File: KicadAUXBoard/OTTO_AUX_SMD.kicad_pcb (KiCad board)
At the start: 2 copper layers, 297 x 92 mm, 203 parts, among them CN203 Conn_01x06, J1_KD028QVFMA17 Conn_02x25_Counter_Clockwise, SW1 ALPS SKHC, SW10 ALPS SKHC, SW11 ALPS SKHC, SW12 ALPS SKHC, SW13 ALPS SKHC, SW14 ALPS SKHC, SW15 ALPS SKHC, SW16 ALPS SKHC, SW17 ALPS SKHC, SW18 ALPS SKHC, SW19 ALPS SKHC, SW2 ALPS SKHC, SW20 ALPS SKHC, SW21 ALPS SKHC, SW22 ALPS SKHC, SW23 ALPS SKHC, SW24 ALPS SKHC, SW25 ALPS SKHC, SW26 ALPS SKHC, SW27 6x6x13mm, SW28 6x6x13mm, SW29 6x6x13mm, SW3 ALPS SKHC, SW30 6x6x13mm, SW31 6x6x13mm, SW32 6x6x13mm, SW33 6x6x13mm, SW34 6x6x13mm, SW35 6x6x13mm, SW36 6x6x13mm, SW37 6x6x13mm, SW38 6x6x13mm, SW39 6x6x13mm, SW4 ALPS SKHC, SW40 6x6x13mm, SW41 6x6x13mm, SW42 6x6x13mm, SW43 6x6x13mm, SW44 6x6x13mm, SW45 6x6x13mm, SW46 6x6x13mm, SW47 6x6x13mm, SW5 ALPS SKHC, SW50 6x6x13mm, SW51 6x6x13mm, SW52 6x6x13mm, SW53 6x6x13mm, SW54 6x6x13mm, SW55 6x6x13mm, SW56 6x6x13mm, SW6 ALPS SKHC, SW7 ALPS SKHC, SW8 ALPS SKHC, SW9 ALPS SKHC, U1 SN74LV1T34_SOT-23_A

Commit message: [AUX] Expand SKHC footprints and move lower keys down
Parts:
- moved LED1 2.04 mm to (54.0, 181.8)
- moved LED10 2.04 mm to (216.0, 181.8)
- moved LED11 2.04 mm to (234.0, 181.8)
- moved LED12 2.04 mm to (252.0, 181.8)
- moved LED13 2.04 mm to (270.0, 181.8)
- moved LED14 2.04 mm to (288.0, 181.8)
- moved LED15 2.04 mm to (306.0, 181.8)
- moved LED16 2.04 mm to (324.0, 181.8)
- moved LED2 2.04 mm to (72.0, 181.8)
- moved LED3 2.04 mm to (90.0, 181.8)
- moved LED4 2.04 mm to (108.0, 181.8)
- moved LED5 2.04 mm to (126.0, 181.8)
- moved LED6 2.04 mm to (144.0, 181.8)
- moved LED7 2.04 mm to (162.0, 181.8)
- moved LED8 2.04 mm to (180.0, 181.8)
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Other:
- outline, holes or cut-outs redrawn

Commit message: Screen backlight control (+more)
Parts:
- moved H201 3.00 mm to (44.8, 195.2)
- moved H202 3.00 mm to (333.2, 195.2)
- moved DISPLAY1 2.96 mm to (207.1, 120.3)
- moved J1_KD028QVFMA17 2.96 mm to (216.9, 132.7)
- moved C78 2.92 mm to (56.6, 169.3)
- moved R11 2.92 mm to (63.5, 168.8)
- moved R208 2.92 mm to (63.5, 166.9)
- moved R27 2.92 mm to (63.5, 170.7)
- moved U1 2.92 mm to (59.6, 169.3)
- moved C1 2.00 mm to (54.0, 177.0)
- moved C10 2.00 mm to (216.0, 177.0)
- moved C11 2.00 mm to (234.0, 177.0)
- moved C12 2.00 mm to (252.0, 177.0)
- moved C13 2.00 mm to (270.0, 177.0)
- moved C14 2.00 mm to (288.0, 177.0)
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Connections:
- LED17 pad 4: /MCU/LEDS/LED_IN -> (no net)
- LED26 pad 1: /MCU/LEDS/LED_CONN1 -> (no net)
- LED27 pad 4: /MCU/LEDS/LED_CONN2 -> (no net)
- LED35 pad 1: Net-(LED34-Pad4) -> (no net)
- LED38 pad 4: Net-(LED38-Pad4) -> (no net)
- LED40 pad 1: Net-(LED39-Pad4) -> (no net)
- LED47 pad 1: /MCU/LEDS/LED_CONN3 -> (no net)
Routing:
- net (no net): track 0.00 -> 492.8 mm
- net /MCU/LEDS/LED_CONN1: track 259.7 -> 0.00 mm
- net /MCU/LEDS/LED_CONN2: track 89.2 -> 0.00 mm
- net /MCU/LEDS/LED_CONN3: track 85.9 -> 0.00 mm
- net Net-(LED38-Pad4): track 22.9 -> 0.00 mm
- net Net-(LED39-Pad4): track 16.9 -> 0.00 mm
- net Net-(LED34-Pad4): track 16.9 -> 0.00 mm
- net GND: track 0.00 -> 3.78 mm
- net +5V_LEDS: track 263.4 -> 265.1 mm
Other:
- board size 297 x 92 mm -> 297 x 95 mm

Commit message: 3d models
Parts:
- removed CN203: Conn_01x06, Connector_PinSocket_2.54mm:PinSocket_1x06_P2.54mm_Vertical
- removed JP1, JP2, JP3: Jumper_2_Open, Jumper:SolderJumper-2_P1.3mm_Open_TrianglePad1.0x1.5mm
- removed R27: 100, Resistor_SMD:R_0805_2012Metric_Pad1.15x1.40mm_HandSolder
- removed TP1: TestPoint, TestPoint:TestPoint_THTPad_D2.0mm_Drill1.0mm
- added C49: 47uF, Capacitor_SMD:C_1206_3216Metric, F.Cu at (56.2, 51.4)
- added C50: 10nF, Capacitor_SMD:C_0805_2012Metric_Pad1.15x1.40mm_HandSolder, F.Cu at (61.4, 51.2)
- added J1: Conn_02x05_Odd_Even, Connector_PinHeader_1.27mm:PinHeader_2x05_P1.27mm_Vertical, B.Cu at (22.7, 77.8)
- added J2: Conn_02x05_Odd_Even, Connector_PinHeader_1.27mm:PinHeader_2x05_P1.27mm_Vertical, B.Cu at (217.9, 74.6)
- added Q1: AO3400A, Package_TO_SOT_SMD:SOT-23, F.Cu at (208.8, 69.5)
- added R1: 47k, Resistor_SMD:R_0805_2012Metric_Pad1.15x1.40mm_HandSolder, F.Cu at (211.6, 69.5)
- added R2: 90, Resistor_SMD:R_0805_2012Metric_Pad1.15x1.40mm_HandSolder, F.Cu at (213.7, 65.1)
- added R3: 100k, Resistor_SMD:R_0805_2012Metric_Pad1.15x1.40mm_HandSolder, F.Cu at (66.1, 51.2)
- added R4: 0, Resistor_SMD:R_0805_2012Metric_Pad1.15x1.40mm_HandSolder, F.Cu at (60.5, 59.1)
- added R5: 90, Resistor_SMD:R_0805_2012Metric_Pad1.15x1.40mm_HandSolder, F.Cu at (203.7, 65.1)
- added R6: 90, Resistor_SMD:R_0805_2012Metric_Pad1.15x1.40mm_HandSolder, F.Cu at (205.7, 65.1)
- added R7: 90, Resistor_SMD:R_0805_2012Metric_Pad1.15x1.40mm_HandSolder, F.Cu at (207.7, 65.1)
- added R8: 90, Resistor_SMD:R_0805_2012Metric_Pad1.15x1.40mm_HandSolder, F.Cu at (209.7, 65.1)
- added R9: 90, Resistor_SMD:R_0805_2012Metric_Pad1.15x1.40mm_HandSolder, F.Cu at (211.7, 65.1)
- added U2: TPS22918_SOT23-6_A, OTTO_Footprints_Lib:SOT-23-6, F.Cu at (55.8, 55.3)
- moved C1 98.9 mm to (26.2, 82.1)
- moved C10 98.9 mm to (188.2, 82.1)
- moved C100 98.9 mm to (231.2, 16.9)
- moved C101 98.9 mm to (243.2, 16.9)
- moved C102 98.9 mm to (255.2, 16.9)
- moved C103 98.9 mm to (267.2, 16.9)
- moved C104 98.9 mm to (285.2, 16.9)
- moved C105 98.9 mm to (297.2, 16.9)
- moved C11 98.9 mm to (206.2, 82.1)
- moved C12 98.9 mm to (224.2, 82.1)
- moved C13 98.9 mm to (242.2, 82.1)
- moved C14 98.9 mm to (260.2, 82.1)
- moved C15 98.9 mm to (278.2, 82.1)
- moved C16 98.9 mm to (296.2, 82.1)
- moved C17 98.9 mm to (53.2, 67.1)
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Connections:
- net /MCU/LEDS/SPI_MOSI_MCU_5V renamed /LEDs/SPI_MOSI_MCU_5V
- J1_KD028QVFMA17 pad 43: BL_PWM -> 5V_BACKLIGHT
- J1_KD028QVFMA17 pad 44: GND -> Net-(J1_KD028QVFMA17-Pad44)
- J1_KD028QVFMA17 pad 45: GND -> Net-(J1_KD028QVFMA17-Pad45)
- J1_KD028QVFMA17 pad 46: GND -> Net-(J1_KD028QVFMA17-Pad46)
- J1_KD028QVFMA17 pad 47: GND -> Net-(J1_KD028QVFMA17-Pad47)
- J1_KD028QVFMA17 pad 48: GND -> Net-(J1_KD028QVFMA17-Pad48)
- J1_KD028QVFMA17 pad 49: GND -> Net-(J1_KD028QVFMA17-Pad49)
- LED1 pad 4: /MCU/LEDS/LED_CONN1 -> /LEDs/LED_CONN1
- LED16 pad 1: /MCU/LEDS/LED_CONN2 -> /LEDs/LED_CONN2
- LED17 pad 4: (no net) -> /LEDs/LED_IN
- LED26 pad 1: (no net) -> /LEDs/LED_CONN1
- LED27 pad 4: (no net) -> /LEDs/LED_CONN2
- LED35 pad 1: (no net) -> Net-(LED34-Pad4)
- LED38 pad 4: (no net) -> Net-(LED38-Pad4)
- LED40 pad 1: (no net) -> Net-(LED39-Pad4)
- LED47 pad 1: (no net) -> /LEDs/LED_CONN3
- LED48 pad 4: /MCU/LEDS/LED_CONN3 -> /LEDs/LED_CONN3
- LED54 pad 1: /MCU/LEDS/LED_OUT -> (no net)
- R208 pad 1: /MCU/LEDS/LED_IN -> /LEDs/LED_IN
- U1 pad 2: (no net) -> /SPI_MOSI_MCU
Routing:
- net (no net): track 492.8 -> 0.05 mm
- net /LEDs/LED_CONN1: track 0.00 -> 268.3 mm
- net /LEDs/LED_CONN2: track 0.00 -> 90.1 mm
- net /LEDs/LED_CONN3: track 0.00 -> 85.9 mm
- net 5V_BACKLIGHT: track 0.00 -> 58.3 mm
- net 3V3: track 0.00 -> 58.1 mm, vias 0 -> 1
- net GND: track 3.78 -> 61.1 mm, vias 0 -> 14
- net Net-(J1_KD028QVFMA17-Pad49): track 0.00 -> 51.0 mm, vias 0 -> 1
- net Net-(J1_KD028QVFMA17-Pad48): track 0.00 -> 49.3 mm, vias 0 -> 1
- net Net-(J1_KD028QVFMA17-Pad47): track 0.00 -> 47.7 mm, vias 0 -> 1
- net SPI_MOSI_RASPI: track 0.00 -> 46.7 mm
- net Net-(J1_KD028QVFMA17-Pad46): track 0.00 -> 46.1 mm, vias 0 -> 1
- net Net-(J1_KD028QVFMA17-Pad45): track 0.00 -> 44.4 mm, vias 0 -> 1
- net SPI_SCLK_RASPI: track 0.00 -> 44.4 mm
- net SPI_CS_RASPI: track 0.00 -> 43.3 mm
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- added copper zone on B.Cu, net GND
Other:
- outline, holes or cut-outs redrawn
- board text removed: "BOOT 0/1"
- board text removed: "JTAG/SWD"
- board text removed: "PO PI/LED"
- board text removed: "STATUS"

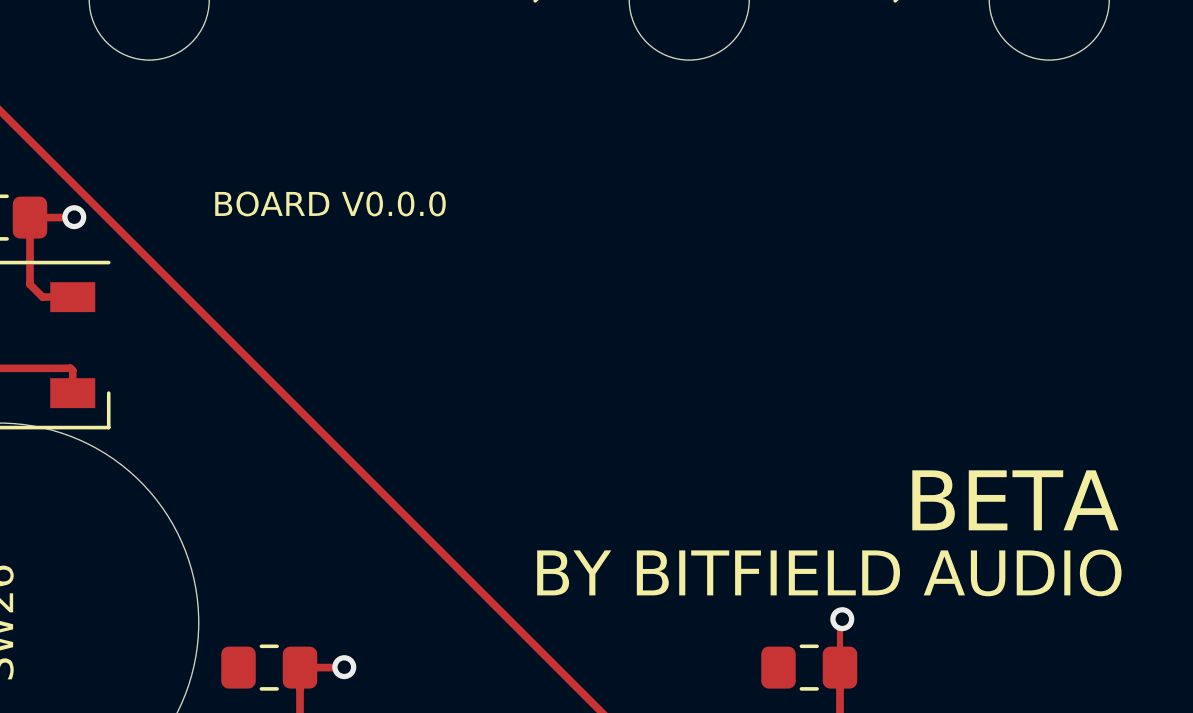
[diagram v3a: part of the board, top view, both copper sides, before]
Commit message: Add simple front pnael
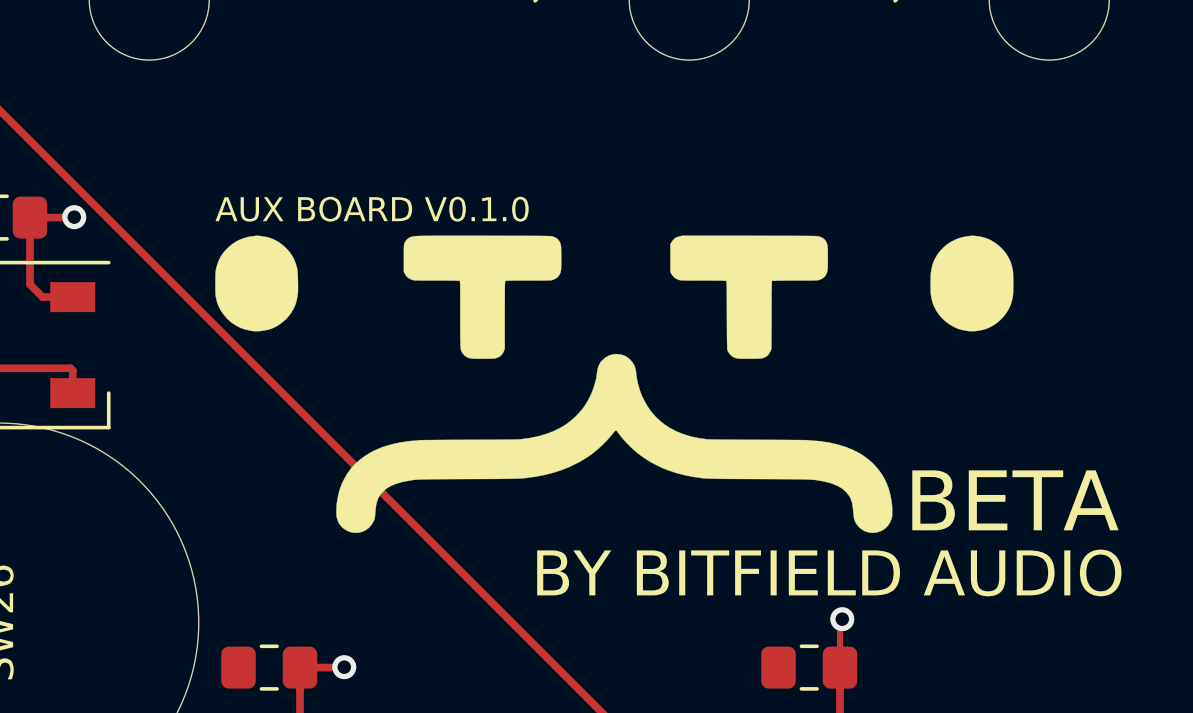
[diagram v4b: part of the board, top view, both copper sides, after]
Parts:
- added G***: otto_logo, OTTO_Footprints_Lib:otto_logo_small, F.Cu at (289.8, 72.8)
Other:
- board text added: "AUX BOARD V0.1.0"
- board text removed: "BOARD V0.0.0"

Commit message: Added front panel and shrunk board width
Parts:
- removed G***: otto_logo, OTTO_Footprints_Lib:otto_logo_small
- moved H213 106.2 mm to (-65.5, 98.1)
- moved J2 105.7 mm to (132.5, 12.4), turned to 270 degrees
- moved R1 96.6 mm to (129.6, 18.4), turned to 0 degrees
- moved Q1 96.3 mm to (125.8, 20.6), turned to 0 degrees
- moved R2 95.1 mm to (129.6, 20.6), turned to 180 degrees
- moved R9 92.4 mm to (129.6, 22.6), turned to 180 degrees
- moved R8 89.7 mm to (129.6, 24.6), turned to 180 degrees
- moved R7 87.1 mm to (129.6, 26.6), turned to 180 degrees
- moved R6 84.4 mm to (129.6, 28.6), turned to 180 degrees
- moved R5 81.7 mm to (129.6, 30.6), turned to 180 degrees
- moved H215 77.4 mm to (-58.5, 98.1)
- moved C48 73.6 mm to (130.1, 48.1), turned to 180 degrees
- moved J1_KD028QVFMA17 43.8 mm to (145.3, 39.9)
- moved R3 39.2 mm to (30.3, 67.0), turned to 90 degrees
- moved C50 33.8 mm to (33.2, 70.0), turned to 180 degrees
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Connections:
- J1 pad 3: LED_PWR_EN -> /SPI_MOSI_MCU
- J1 pad 4: /SPI_MOSI_MCU -> LED_PWR_EN
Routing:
- net Net-(J1_KD028QVFMA17-Pad49): track 51.0 -> 17.1 mm
- net Net-(J1_KD028QVFMA17-Pad48): track 49.3 -> 16.5 mm
- net Net-(J1_KD028QVFMA17-Pad47): track 47.7 -> 15.9 mm
- net 5V_BACKLIGHT: track 58.3 -> 27.3 mm
- net Net-(J1_KD028QVFMA17-Pad46): track 46.1 -> 15.3 mm
- net Net-(J1_KD028QVFMA17-Pad45): track 44.4 -> 14.6 mm
- net Net-(J1_KD028QVFMA17-Pad44): track 42.8 -> 14.0 mm
- net 3V3: track 58.1 -> 77.7 mm
- net /SPI_MOSI_MCU: track 0.00 -> 18.9 mm
- net +5V_REG: track 0.00 -> 16.6 mm
- net LED_PWR_EN: track 0.00 -> 15.8 mm, vias 0 -> 1
- net +5V_LEDS: track 265.1 -> 278.5 mm, vias 54 -> 57
- net BL_PWM: track 6.41 -> 18.0 mm
- net /LEDs/SPI_MOSI_MCU_5V: track 0.00 -> 7.63 mm
- net SPI_MOSI_RASPI: track 46.7 -> 41.8 mm
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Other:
- board size 297 x 95 mm -> 288.5 x 95 mm
- board text removed: "SCREEN"

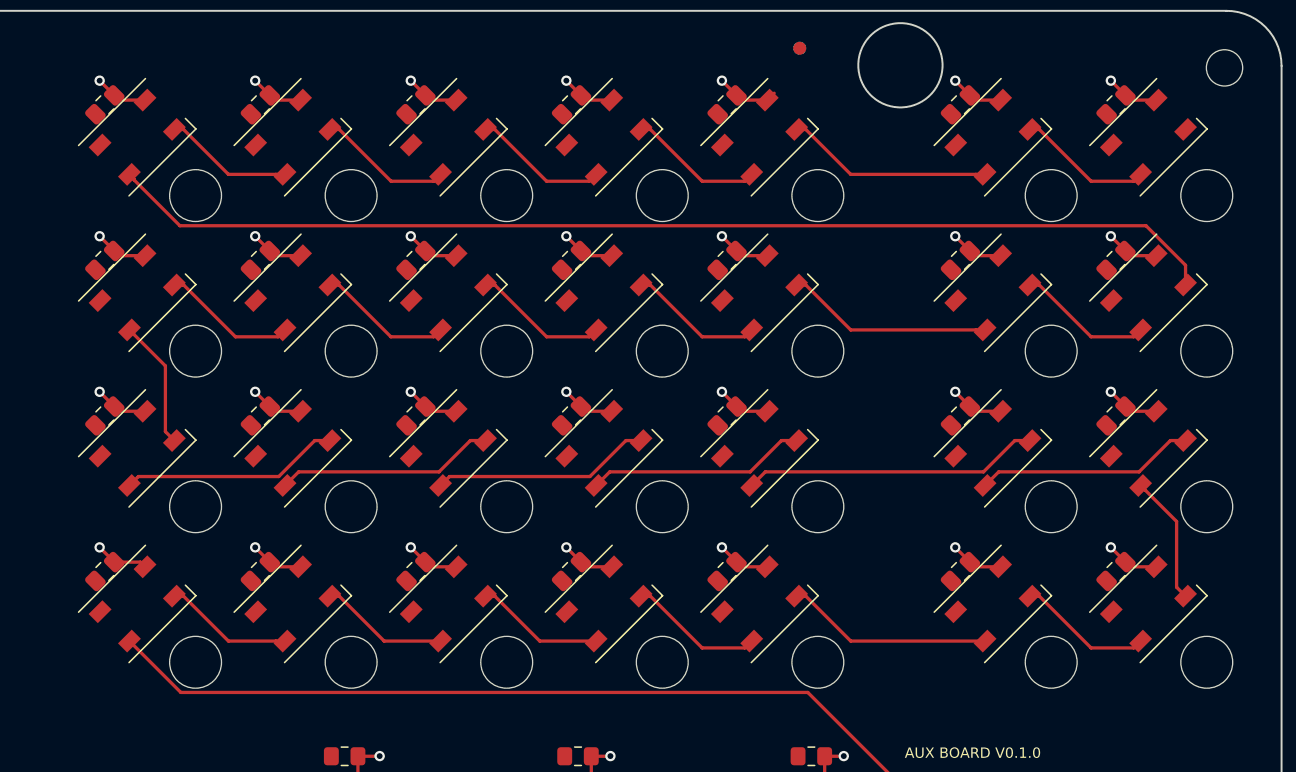
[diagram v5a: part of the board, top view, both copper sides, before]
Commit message: Moved LEDs closer to buttons
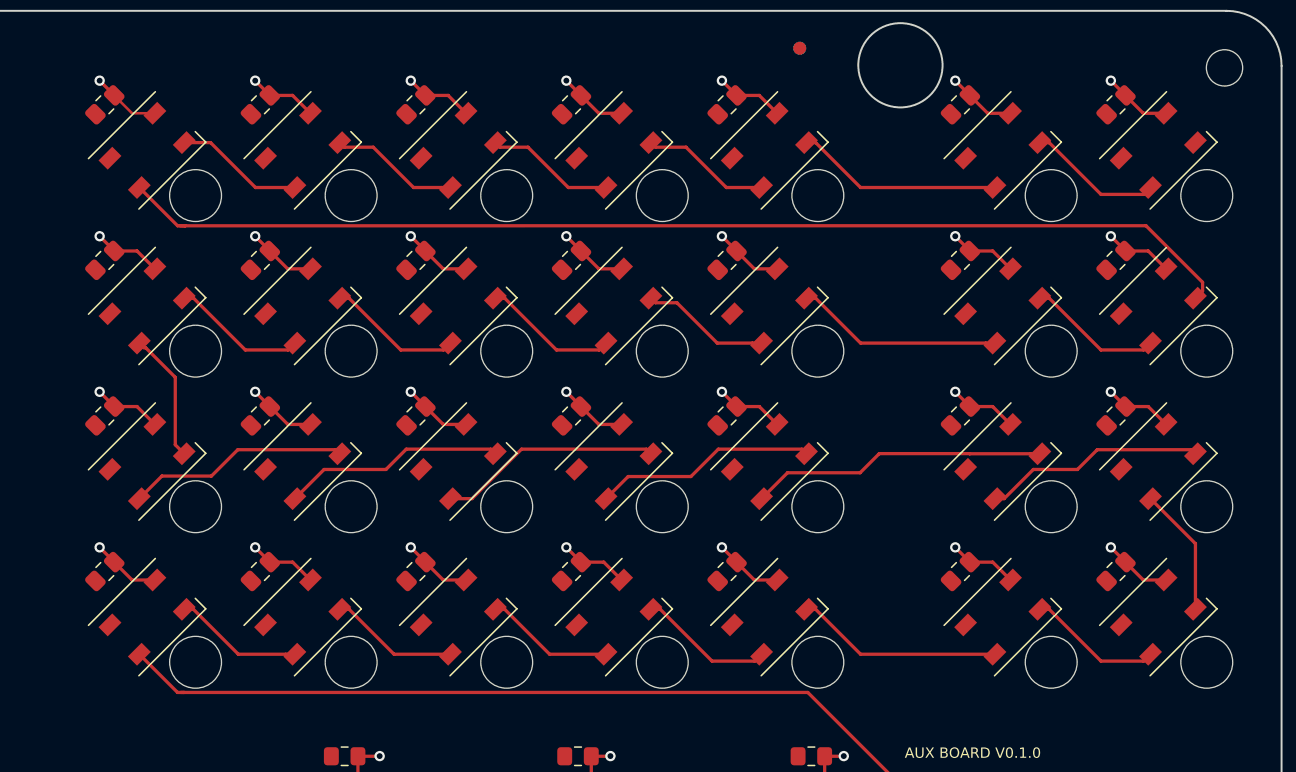
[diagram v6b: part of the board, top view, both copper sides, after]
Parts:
- moved LED27 1.27 mm to (218.0, 56.4)
- moved LED28 1.27 mm to (230.0, 56.4)
- moved LED29 1.27 mm to (242.0, 56.4)
- moved LED30 1.27 mm to (254.0, 56.4)
- moved LED31 1.27 mm to (266.0, 56.4)
- moved LED32 1.27 mm to (284.0, 56.4)
- moved LED33 1.27 mm to (296.0, 56.4)
- moved LED34 1.27 mm to (218.0, 44.4)
- moved LED35 1.27 mm to (230.0, 44.4)
- moved LED36 1.27 mm to (242.0, 44.4)
- moved LED37 1.27 mm to (254.0, 44.4)
- moved LED38 1.27 mm to (266.0, 44.4)
- moved LED39 1.27 mm to (284.0, 44.4)
- moved LED40 1.27 mm to (296.0, 44.4)
- moved LED41 1.27 mm to (218.0, 32.4)
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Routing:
- net +5V_LEDS: track 278.5 -> 324.6 mm
- net /LEDs/LED_CONN3: track 85.9 -> 86.9 mm
- net /LEDs/LED_CONN2: track 94.6 -> 93.7 mm
